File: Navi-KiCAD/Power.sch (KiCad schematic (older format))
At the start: 19 parts, among them U8 TPS54232DR

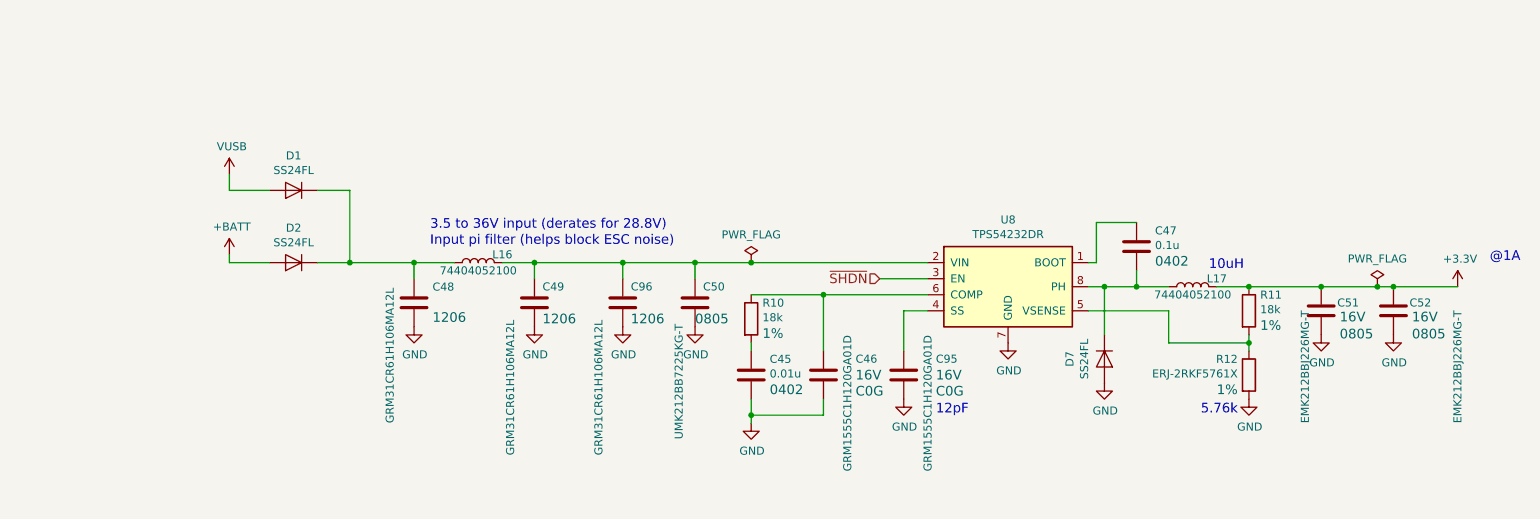
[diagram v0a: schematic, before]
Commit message: Completed key routing.
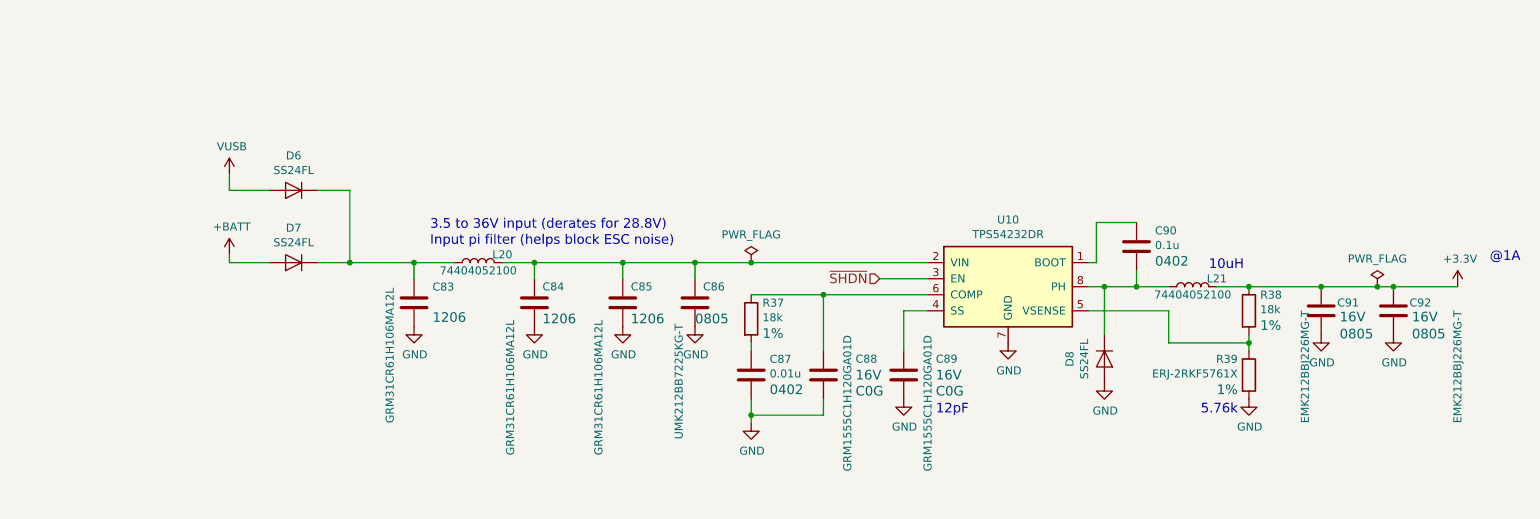
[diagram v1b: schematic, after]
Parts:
- renumbered C48 to C83, C49 to C84, C96 to C85, C50 to C86, C45 to C87, C46 to C88, C95 to C89, C47 to C90, C51 to C91, C52 to C92, D1 to D6, D2 to D7, D7 to D8, L16 to L20, L17 to L21, R10 to R37, R11 to R38, R12 to R39, U8 to U10
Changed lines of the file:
@@
 Input pi filter (helps block ESC noise)
 $Comp
-L L L16
+L L L20
 U 1 1 58AC1391
 P 3550 3750
-F 0 "L16" V 3600 3600 50  0000 C CNN
+F 0 "L20" V 3600 3600 50  0000 C CNN
 F 1 "74404052100" V 3500 3750 50  0000 C CNN
 F 2 "Inductors:Inductor_Wurth_LQS-5020" H -1600 450 50  0001 C CNN
@@
 3.5 to 36V input (derates for 28.8V)
 $Comp
-L D D1
+L D D6
 U 1 1 58B2E19A
 P 2400 3300
-F 0 "D1" H 2400 3084 50  0000 C CNN
+F 0 "D6" H 2400 3084 50  0000 C CNN
 F 1 "SS24FL" H 2400 3175 50  0000 C CNN
 F 2 "Diodes_SMD:D_SOD-123F" H 1100 1350 50  0001 C CNN
@@
 $EndComp
 $Comp
-L D D2
+L D D7
 U 1 1 58B2EA81
 P 2400 3750
-F 0 "D2" H 2400 3534 50  0000 C CNN
+F 0 "D7" H 2400 3534 50  0000 C CNN
 F 1 "SS24FL" H 2400 3625 50  0000 C CNN
 F 2 "Diodes_SMD:D_SOD-123F" H 1100 1800 50  0001 C CNN
@@
 $EndComp
 $Comp
-L C C48
+L C C83
 U 1 1 58B724AF
 P 3150 4000
-F 0 "C48" H 3265 4099 50  0000 L CNN
+F 0 "C83" H 3265 4099 50  0000 L CNN
 F 1 "GRM31CR61H106MA12L" V 3000 3250 50  0000 L CNN
 F 2 "Capacitors_SMD:C_1206" H 1288 -400 50  0001 C CNN
@@
 $EndComp
 $Comp
-L C C49
+L C C84
 U 1 1 58B727EB
 P 3900 4000
-F 0 "C49" H 3950 4100 50  0000 L CNN
+F 0 "C84" H 3950 4100 50  0000 L CNN
 F 1 "GRM31CR61H106MA12L" V 3750 3050 50  0000 L CNN
 F 2 "Capacitors_SMD:C_1206" H 2038 -400 50  0001 C CNN
@@
 $EndComp
 $Comp
-L C C50
+L C C86
 U 1 1 58B72ACD
 P 4900 4000
-F 0 "C50" H 4950 4100 50  0000 L CNN
+F 0 "C86" H 4950 4100 50  0000 L CNN
 F 1 "UMK212BB7225KG-T" V 4800 3150 50  0000 L CNN
 F 2 "Capacitors_SMD:C_0805" H 3038 -400 50  0001 C CNN
@@
 $EndComp
 $Comp
-L R R10
+L R R37
 U 1 1 58B73150
 P 5250 4100
-F 0 "R10" H 5320 4199 50  0000 L CNN
+F 0 "R37" H 5320 4199 50  0000 L CNN
 F 1 "18k" H 5320 4108 50  0000 L CNN
 F 2 "Resistors_SMD:R_0402" V 450 1450 50  0001 C CNN
@@
 $EndComp
 $Comp
-L C C45
+L C C87
 U 1 1 58B73331
 P 5250 4450
-F 0 "C45" H 5365 4549 50  0000 L CNN
+F 0 "C87" H 5365 4549 50  0000 L CNN
 F 1 "0.01u" H 5365 4458 50  0000 L CNN
 F 2 "Capacitors_SMD:C_0402" H 3388 50  50  0001 C CNN
@@
 $EndComp
 $Comp
-L C C47
+L C C90
 U 1 1 58B74095
 P 7650 3650
-F 0 "C47" H 7535 3551 50  0000 R CNN
+F 0 "C90" H 7535 3551 50  0000 R CNN
 F 1 "0.1u" H 7535 3642 50  0000 R CNN
 F 2 "Capacitors_SMD:C_0402" H 5788 -750 50  0001 C CNN
@@
 $EndComp
 $Comp
-L C C51
+L C C91
 U 1 1 58B74812
 P 8800 4050
-F 0 "C51" H 8900 4100 50  0000 L CNN
+F 0 "C91" H 8900 4100 50  0000 L CNN
 F 1 "EMK212BBJ226MG-T" V 8700 3350 50  0000 L CNN
 F 2 "Capacitors_SMD:C_0805" H 6938 -350 50  0001 C CNN
@@
 $EndComp
 $Comp
-L C C52
+L C C92
 U 1 1 58B74BDA
 P 9250 4050
-F 0 "C52" H 9350 4100 50  0000 L CNN
+F 0 "C92" H 9350 4100 50  0000 L CNN
 F 1 "EMK212BBJ226MG-T" V 9650 3350 50  0000 L CNN
 F 2 "Capacitors_SMD:C_0805" H 7388 -350 50  0001 C CNN
@@
 $EndComp
 $Comp
-L TPS54232 U8
+L TPS54232 U10
 U 1 1 58E2B6C6
 P 6850 3900
-F 0 "U8" H 6850 4317 50  0000 C CNN
+F 0 "U10" H 6850 4317 50  0000 C CNN
 F 1 "TPS54232DR" H 6850 4226 50  0000 C CNN
 F 2 "Housings_SOIC:SOIC-8_3.9x4.9mm_Pitch1.27mm" H -800 2750 50  0001 L CNN
@@
 	6200 4050 6350 4050
 $Comp
-L C C95
+L C C89
 U 1 1 58E2F44B
 P 6200 4450
-F 0 "C95" H 6000 4350 50  0000 R CNN
+F 0 "C89" H 6000 4350 50  0000 R CNN
 F 1 "GRM1555C1H120GA01D" V 6050 5050 50  0000 R CNN
 F 2 "Capacitors_SMD:C_0402" H 1488 3000 50  0001 C CNN
@@
 12pF
 $Comp
-L R R11
+L R R38
 U 1 1 58E2FAEC
 P 8350 4050
-F 0 "R11" H 8420 4149 50  0000 L CNN
+F 0 "R38" H 8420 4149 50  0000 L CNN
 F 1 "18k" H 8420 4058 50  0000 L CNN
 F 2 "Resistors_SMD:R_0402" V 3550 1400 50  0001 C CNN
@@
 $EndComp
 $Comp
-L R R12
+L R R39
 U 1 1 58E2FC46
 P 8350 4450
-F 0 "R12" H 8280 4549 50  0000 R CNN
+F 0 "R39" H 8280 4549 50  0000 R CNN
 F 1 "ERJ-2RKF5761X" H 8280 4458 50  0000 R CNN
 F 2 "Resistors_SMD:R_0402" V 3550 1800 50  0001 C CNN
@@
 $EndComp
 $Comp
-L D D7
+L D D8
 U 1 1 58E32A60
 P 7450 4350
-F 0 "D7" H 7450 4134 50  0000 C CNN
+F 0 "D8" H 7450 4134 50  0000 C CNN
 F 1 "SS24FL" H 7450 4225 50  0000 C CNN
 F 2 "Diodes_SMD:D_SOD-123F" H 6150 2400 50  0001 C CNN
@@
 	7400 3750 7350 3750
 $Comp
-L C C46
+L C C88
 U 1 1 58E34840
 P 5700 4450
-F 0 "C46" H 5500 4350 50  0000 R CNN
+F 0 "C88" H 5500 4350 50  0000 R CNN
 F 1 "GRM1555C1H120GA01D" V 5550 5050 50  0000 R CNN
 F 2 "Capacitors_SMD:C_0402" H 988 3000 50  0001 C CNN
@@
 Connection ~ 5250 3750
 $Comp
-L L L17
+L L L21
 U 1 1 58E46EFA
 P 8000 3900
-F 0 "L17" V 8050 3750 50  0000 C CNN
+F 0 "L21" V 8050 3750 50  0000 C CNN
 F 1 "74404052100" V 7950 3900 50  0000 C CNN
 F 2 "Inductors:Inductor_Wurth_LQS-5020" H 2850 600 50  0001 C CNN
@@
 $EndComp
 $Comp
-L C C96
+L C C85
 U 1 1 58E4E122
 P 4450 4000
-F 0 "C96" H 4500 4100 50  0000 L CNN
+F 0 "C85" H 4500 4100 50  0000 L CNN
 F 1 "GRM31CR61H106MA12L" V 4300 3050 50  0000 L CNN
 F 2 "Capacitors_SMD:C_1206" H 2588 -400 50  0001 C CNN

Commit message: Some more GNC processor routing
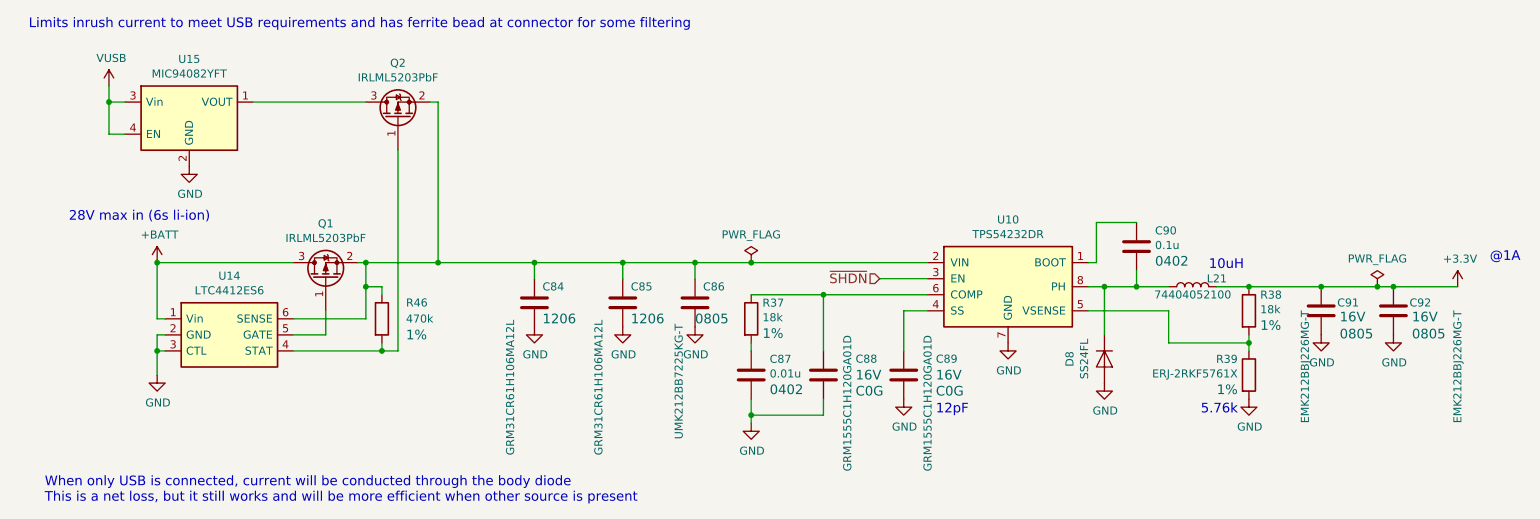
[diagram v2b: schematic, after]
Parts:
- removed C83: GRM31CR61H106MA12L, Capacitors_SMD:C_1206, symbol C
- removed D6, D7: SS24FL, Diodes_SMD:D_SOD-123F, symbol D
- removed L20: 74404052100, Inductors:Inductor_Wurth_LQS-5020, symbol L
- added Q1, Q2: IRLML5203PbF, TO_SOT_Packages_SMD:SOT-23, symbol Q_PMOS_GSD
- added R46: 470k, Resistors_SMD:R_0402, symbol R
- added U14: LTC4412ES6, TO_SOT_Packages_SMD:TSOT-23-6_MK06A, symbol LTC4412
- added U15: MIC94082YFT, SMD_Packages:TMLF085085D-4LD-9, symbol MIC94082YFT
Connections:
- net +BATT: now also Q1.3 (D), U14.1 (Vin)
- net GND: now also U14.2 (GND), U14.3 (CTL), U15.2 (GND)
- net VUSB: now also U15.3 (Vin), U15.4 (EN)
- net at C84.1, C85.1, C86.1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: now also Q1.2 (S), Q2.2 (S), R46.1, U14.6 (SENSE)
- new net: Q2.1 (G), R46.2, U14.4 (STAT)
- new net: Q1.1 (G), U14.5 (GATE)
- new net: Q2.3 (D), U15.1 (VOUT)
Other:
- note added: "28V max in (6s li-ion)"
- note added: "Limits inrush current to meet USB requirements and has ferrite bead at connector for some filtering"
- note added: "When only USB is connected, current will be conducted through the body diode\nThis is a net loss, but it still works and will be more efficient when other source is present"
- note removed: "3.5 to 36V input (derates for 28.8V)"
- note removed: "Input pi filter (helps block ESC noise)"
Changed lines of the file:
@@
 EESchema Schematic File Version 2
-LIBS:Navi-rescue
 LIBS:device
 LIBS:rfcom
@@
 LIBS:powerint
 LIBS:onsemi
+LIBS:transistors
+LIBS:ESD_Protection
+LIBS:ftdi
+LIBS:stm32
+LIBS:transf
+LIBS:ttl_ieee
 LIBS:Navi-cache
 EELAYER 26 0
@@
 $EndDescr
 $Comp
-L +3.3V #PWR0123
+L +3.3V #PWR0124
 U 1 1 58AB9BA4
 P 9650 3900
-F 0 "#PWR0123" H 4650 800 50  0001 C CNN
+F 0 "#PWR0124" H 4650 800 50  0001 C CNN
 F 1 "+3.3V" H 9665 4073 50  0000 C CNN
 F 2 "" H 4650 950 50  0001 C CNN
@@
 ~SHDN
 $Comp
-L GND #PWR0124
+L GND #PWR0125
 U 1 1 58ABCF35
 P 4900 4150
-F 0 "#PWR0124" H 1650 -650 50  0001 C CNN
+F 0 "#PWR0125" H 1650 -650 50  0001 C CNN
 F 1 "GND" H 4905 3977 50  0000 C CNN
 F 2 "" H 1650 -400 50  0001 C CNN
@@
 $EndComp
 $Comp
-L GND #PWR0125
+L GND #PWR0126
 U 1 1 58ABD05E
 P 3900 4150
-F 0 "#PWR0125" H 650 -650 50  0001 C CNN
+F 0 "#PWR0126" H 650 -650 50  0001 C CNN
 F 1 "GND" H 3905 3977 50  0000 C CNN
 F 2 "" H 650 -400 50  0001 C CNN
@@
 	5250 3950 6350 3950
 Wire Wire Line
-	3700 3750 6350 3750
+	2800 3750 6350 3750
 Wire Wire Line
 	5250 4300 5250 4250
@@
 	3900 3850 3900 3750
 Connection ~ 3900 3750
-$Comp
-L GND #PWR0126
-U 1 1 58ABDCB9
-P 3150 4150
-F 0 "#PWR0126" H -100 -650 50  0001 C CNN
-F 1 "GND" H 3155 3977 50  0000 C CNN
-F 2 "" H -100 -400 50  0001 C CNN
-F 3 "" H -100 -400 50  0001 C CNN
-	1    3150 4150
-	1    0    0    -1
-$EndComp
-Wire Wire Line
-	2550 3750 3400 3750
-Wire Wire Line
-	3150 3750 3150 3850
-Connection ~ 3150 3750
-Text Notes 3250 3650 0    60   ~ 0
-Input pi filter (helps block ESC noise)
-$Comp
-L L L20
-U 1 1 58AC1391
-P 3550 3750
-F 0 "L20" V 3600 3600 50  0000 C CNN
-F 1 "74404052100" V 3500 3750 50  0000 C CNN
-F 2 "Inductors:Inductor_Wurth_LQS-5020" H -1600 450 50  0001 C CNN
-F 3 "http://katalog.we-online.de/pbs/datasheet/74404052100.pdf" H -1600 450 50  0001 C CNN
-	1    3550 3750
-	0    -1   -1   0
-$EndComp
 Text Notes 9850 3750 0    60   ~ 0
 @1A
-Text Notes 3250 3550 0    60   ~ 0
-3.5 to 36V input (derates for 28.8V)
-$Comp
-L D D6
-U 1 1 58B2E19A
-P 2400 3300
-F 0 "D6" H 2400 3084 50  0000 C CNN
-F 1 "SS24FL" H 2400 3175 50  0000 C CNN
-F 2 "Diodes_SMD:D_SOD-123F" H 1100 1350 50  0001 C CNN
-F 3 "http://www.onsemi.com/pub/Collateral/NTS245SF-D.PDF" H 1100 1350 50  0001 C CNN
-	1    2400 3300
-	-1   0    0    1
-$EndComp
-Wire Wire Line
-	2550 3300 2750 3300
-Wire Wire Line
-	2750 3300 2750 3750
-Connection ~ 2750 3750
-Wire Wire Line
-	2250 3750 2000 3750
-Wire Wire Line
-	2000 3750 2000 3700
-Wire Wire Line
-	2250 3300 2000 3300
-Wire Wire Line
-	2000 3300 2000 3200
+Wire Wire Line
+	3250 2750 3300 2750
+Wire Wire Line
+	3300 2750 3300 3750
+Connection ~ 3300 3750
 $Comp
 L +BATT #PWR0127
 U 1 1 58B2E558
-P 2000 3700
-F 0 "#PWR0127" H 950 800 50  0001 C CNN
-F 1 "+BATT" H 2015 3873 50  0000 C CNN
-F 2 "" H 950 950 50  0001 C CNN
-F 3 "" H 950 950 50  0001 C CNN
-	1    2000 3700
+P 1550 3750
+F 0 "#PWR0127" H 500 850 50  0001 C CNN
+F 1 "+BATT" H 1565 3923 50  0000 C CNN
+F 2 "" H 500 1000 50  0001 C CNN
+F 3 "" H 500 1000 50  0001 C CNN
+	1    1550 3750
 	1    0    0    -1
 $EndComp
@@
 L VUSB #PWR0128
 U 1 1 58B2E98C
-P 2000 3200
-F 0 "#PWR0128" H 850 1100 50  0001 C CNN
-F 1 "VUSB" H 2015 3373 50  0000 C CNN
-F 2 "" H 850 1250 50  0001 C CNN
-F 3 "" H 850 1250 50  0001 C CNN
-	1    2000 3200
-	1    0    0    -1
-$EndComp
-$Comp
-L D D7
-U 1 1 58B2EA81
-P 2400 3750
-F 0 "D7" H 2400 3534 50  0000 C CNN
-F 1 "SS24FL" H 2400 3625 50  0000 C CNN
-F 2 "Diodes_SMD:D_SOD-123F" H 1100 1800 50  0001 C CNN
-F 3 "http://www.onsemi.com/pub/Collateral/NTS245SF-D.PDF" H 1100 1800 50  0001 C CNN
-	1    2400 3750
-	-1   0    0    1
-$EndComp
-$Comp
-L C C83
-U 1 1 58B724AF
-P 3150 4000
-F 0 "C83" H 3265 4099 50  0000 L CNN
-F 1 "GRM31CR61H106MA12L" V 3000 3250 50  0000 L CNN
-F 2 "Capacitors_SMD:C_1206" H 1288 -400 50  0001 C CNN
-F 3 "" H 1250 -250 50  0001 C CNN
-F 4 "50V" H 1350 -300 60  0001 L CNN "Voltage"
-F 5 "20%" H 1350 -200 60  0001 L CNN "Tolerance"
-F 6 "X7R" H 1300 -100 60  0001 L CNN "Type"
-F 7 "1206" H 3265 3909 60  0000 L CNN "Package"
-	1    3150 4000
+P 1250 2650
+F 0 "#PWR0128" H 100 550 50  0001 C CNN
+F 1 "VUSB" H 1265 2823 50  0000 C CNN
+F 2 "" H 100 700 50  0001 C CNN
+F 3 "" H 100 700 50  0001 C CNN
+	1    1250 2650
 	1    0    0    -1
 $EndComp
@@
 	4450 3850 4450 3750
 Connection ~ 4450 3750
+$Comp
+L LTC4412 U14
+U 1 1 58CF19E6
+P 2000 4200
+F 0 "U14" H 2000 4567 50  0000 C CNN
+F 1 "LTC4412ES6" H 2000 4476 50  0000 C CNN
+F 2 "TO_SOT_Packages_SMD:TSOT-23-6_MK06A" H -350 1750 50  0001 L CNN
+F 3 "http://cds.linear.com/docs/en/datasheet/4412fb.pdf" H 700 1650 50  0001 C CNN
+	1    2000 4200
+	1    0    0    -1
+$EndComp
+Text Notes 750  2300 0    60   ~ 0
+Limits inrush current to meet USB requirements and has ferrite bead at connector for some filtering
+$Comp
+L MIC94082YFT U15
+U 1 1 58D00FFA
+P 1750 2850
+F 0 "U15" H 1750 3217 50  0000 C CNN
+F 1 "MIC94082YFT" H 1750 3126 50  0000 C CNN
+F 2 "SMD_Packages:TMLF085085D-4LD-9" H -1800 -500 50  0001 L CNN
+F 3 "http://ww1.microchip.com/downloads/en/DeviceDoc/mic94080_5.pdf" H -750 -600 50  0001 C CNN
+	1    1750 2850
+	1    0    0    -1
+$EndComp
+Wire Wire Line
+	1250 2750 1350 2750
+Wire Wire Line
+	1250 2950 1350 2950
+Connection ~ 1250 2750
+Text Notes 1000 3500 0    60   ~ 0
+28V max in (6s li-ion)
+$Comp
+L GND #PWR0139
+U 1 1 58D02606
+P 1750 3150
+F 0 "#PWR0139" H -1500 -1650 50  0001 C CNN
+F 1 "GND" H 1755 2977 50  0000 C CNN
+F 2 "" H -1500 -1400 50  0001 C CNN
+F 3 "" H -1500 -1400 50  0001 C CNN
+	1    1750 3150
+	1    0    0    -1
+$EndComp
+$Comp
+L Q_PMOS_GSD Q1
+U 1 1 58D0305E
+P 2600 3850
+F 0 "Q1" V 2943 3850 50  0000 C CNN
+F 1 "IRLML5203PbF" V 2852 3850 50  0000 C CNN
+F 2 "TO_SOT_Packages_SMD:SOT-23" H -250 -800 50  0001 C CNN
+F 3 "http://www.infineon.com/dgdl/irlml5203pbf.pdf?fileId=5546d462533600a40153566868da261d" H -450 -900 50  0001 C CNN
+	1    2600 3850
+	0    -1   -1   0
+$EndComp
+Wire Wire Line
+	1550 3750 2400 3750
+Wire Wire Line
+	2150 2750 2850 2750
+Wire Wire Line
+	3050 4300 3050 3050
+Wire Wire Line
+	2400 4300 3050 4300
+Wire Wire Line
+	2400 4200 2600 4200
+Wire Wire Line
+	2600 4200 2600 4050
+Wire Wire Line
+	2850 4100 2400 4100
+Wire Wire Line
+	2850 3750 2850 4100
+Connection ~ 2850 3750
+Wire Wire Line
+	1600 4100 1550 4100
+Wire Wire Line
+	1550 4100 1550 3750
+Connection ~ 1550 3750
+$Comp
+L R R46
+U 1 1 58D04424
+P 2950 4100
+F 0 "R46" H 3100 4200 50  0000 L CNN
+F 1 "470k" H 3100 4100 50  0000 L CNN
+F 2 "Resistors_SMD:R_0402" V -1850 1450 50  0001 C CNN
+F 3 "" V -1570 1450 50  0001 C CNN
+F 4 "1%" H 3100 4000 60  0000 L CNN "Tolerance"
+F 5 "16V" V -1400 1450 60  0001 C CNN "Voltage"
+F 6 "0.062W" V -1300 1450 60  0001 C CNN "Power"
+F 7 "Thin Film" V -1200 1450 60  0001 C CNN "Material"
+F 8 "0402" V -1750 1450 60  0001 C CNN "Package"
+	1    2950 4100
+	1    0    0    -1
+$EndComp
+Wire Wire Line
+	2950 3950 2950 3900
+Wire Wire Line
+	2950 3900 2850 3900
+Connection ~ 2850 3900
+Wire Wire Line
+	2950 4250 2950 4300
+Connection ~ 2950 4300
+Wire Wire Line
+	1550 4450 1550 4200
+Wire Wire Line
+	1550 4200 1600 4200
+$Comp
+L GND #PWR0140
+U 1 1 58D05C20
+P 1550 4450
+F 0 "#PWR0140" H -1700 -350 50  0001 C CNN
+F 1 "GND" H 1555 4277 50  0000 C CNN
+F 2 "" H -1700 -100 50  0001 C CNN
+F 3 "" H -1700 -100 50  0001 C CNN
+	1    1550 4450
+	1    0    0    -1
+$EndComp
+Text Notes 850  5250 0    60   ~ 0
+When only USB is connected, current will be conducted through the body diode\nThis is a net loss, but it still works and will be more efficient when other source is present
+$Comp
+L Q_PMOS_GSD Q2
+U 1 1 58D0ABA0
+P 3050 2850
+F 0 "Q2" V 3393 2850 50  0000 C CNN
+F 1 "IRLML5203PbF" V 3302 2850 50  0000 C CNN
+F 2 "TO_SOT_Packages_SMD:SOT-23" H 200 -1800 50  0001 C CNN
+F 3 "http://www.infineon.com/dgdl/irlml5203pbf.pdf?fileId=5546d462533600a40153566868da261d" H 0   -1900 50  0001 C CNN
+	1    3050 2850
+	0    -1   -1   0
+$EndComp
+Wire Wire Line
+	1250 2950 1250 2650
+Wire Wire Line
+	1600 4300 1550 4300
+Connection ~ 1550 4300
 $EndSCHEMATC

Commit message: Additional routing
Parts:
- Q1, Q2: value IRLML5203PbF -> IRLML5203TRPBF
- U14: value LTC4412ES6 -> LTC4412ES6#TRPBF
- U15: value MIC94082YFT -> MIC94082YFT-TR
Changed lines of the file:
@@
 P 2000 4200
 F 0 "U14" H 2000 4567 50  0000 C CNN
-F 1 "LTC4412ES6" H 2000 4476 50  0000 C CNN
+F 1 "LTC4412ES6#TRPBF" H 2000 4476 50  0000 C CNN
 F 2 "TO_SOT_Packages_SMD:TSOT-23-6_MK06A" H -350 1750 50  0001 L CNN
 F 3 "http://cds.linear.com/docs/en/datasheet/4412fb.pdf" H 700 1650 50  0001 C CNN
@@
 P 1750 2850
 F 0 "U15" H 1750 3217 50  0000 C CNN
-F 1 "MIC94082YFT" H 1750 3126 50  0000 C CNN
+F 1 "MIC94082YFT-TR" H 1750 3126 50  0000 C CNN
 F 2 "SMD_Packages:TMLF085085D-4LD-9" H -1800 -500 50  0001 L CNN
 F 3 "http://ww1.microchip.com/downloads/en/DeviceDoc/mic94080_5.pdf" H -750 -600 50  0001 C CNN
@@
 P 2600 3850
 F 0 "Q1" V 2943 3850 50  0000 C CNN
-F 1 "IRLML5203PbF" V 2852 3850 50  0000 C CNN
+F 1 "IRLML5203TRPBF" V 2852 3850 50  0000 C CNN
 F 2 "TO_SOT_Packages_SMD:SOT-23" H -250 -800 50  0001 C CNN
 F 3 "http://www.infineon.com/dgdl/irlml5203pbf.pdf?fileId=5546d462533600a40153566868da261d" H -450 -900 50  0001 C CNN
@@
 P 3050 2850
 F 0 "Q2" V 3393 2850 50  0000 C CNN
-F 1 "IRLML5203PbF" V 3302 2850 50  0000 C CNN
+F 1 "IRLML5203TRPBF" V 3302 2850 50  0000 C CNN
 F 2 "TO_SOT_Packages_SMD:SOT-23" H 200 -1800 50  0001 C CNN
 F 3 "http://www.infineon.com/dgdl/irlml5203pbf.pdf?fileId=5546d462533600a40153566868da261d" H 0   -1900 50  0001 C CNN
